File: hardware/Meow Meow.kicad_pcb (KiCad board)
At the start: 2 copper layers, 52.5 x 47.5 mm, 22 parts, among them P1 USB_micro, P2 UP, P3 LEFT, P4 CONN_02X03, P5 CLICK_LEFT, P6 RIGHT, P7 SPACE, SW1 RESET, U1 ATSAMD11C14A-SSUT, U2 AP2114-3.3K, Y1 32k

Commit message: Update componets
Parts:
- removed C3: 22pF, Capacitors_SMD:C_0805_HandSoldering
- removed Y1: 32k, Crystals:Crystal_Round_d3.0mm_Vertical
- added F1: 0.5A, Resistors_SMD:R_1812_HandSoldering, F.Cu at (164.0, 99.0)
- added P1: D, MeowMeow:ALLIGATORCLIP, F.Cu at (120.5, 67.7)
- added P10: A, MeowMeow:ALLIGATORCLIP, F.Cu at (145.8, 66.5)
- added P11: W, MeowMeow:ALLIGATORCLIP, F.Cu at (152.8, 67.0)
- added P12: MOUSE_LEFT, MeowMeow:ALLIGATORCLIP, F.Cu at (104.5, 68.0)
- added P13: CONN_01X12, Pin_Headers:Pin_Header_Straight_1x12_Pitch2.54mm, F.Cu at (120.0, 94.2)
- added P8: S, MeowMeow:ALLIGATORCLIP, F.Cu at (125.5, 68.0)
- C1: value 22pF -> C_Small
- D1: value LED -> POWER
- P2: value UP -> SPACE
- P3: value LEFT -> KEY_RIGHT_ARROW
- P5: value CLICK_LEFT -> KEY_LEFT_ARROW
- P6: value RIGHT -> KEY_DOWN_ARROW
- P7: value SPACE -> KEY_UP_ARROW
- P9: renamed from P1; value USB_micro -> USB_Micro
- SW1: value RESET -> SW_Push
- U1: value ATSAMD11C14A-SSUT -> ATSAMD21G15A-AU; footprint Housings_SOIC:SOIC-14_3.9x8.7mm_Pitch1.27mm -> Housings_QFP:TQFP-48_7x7mm_Pitch0.5mm
- moved P2 43.1 mm to (108.0, 67.7), turned to 0 degrees
- moved C2 34.4 mm to (149.0, 101.0)
- moved P7 33.6 mm to (137.8, 68.2)
- moved P6 30.3 mm to (131.5, 67.7)
- moved P5 30.3 mm to (116.2, 68.2)
- moved P3 22.0 mm to (111.0, 68.0)
- moved D2 10.2 mm to (128.0, 112.2)
- moved R3 10.2 mm to (129.3, 109.0)
- moved C1 6.53 mm to (141.5, 94.5), turned to 0 degrees
- moved R1 4.74 mm to (130.8, 120.4)
- moved SW1 4.74 mm to (127.5, 119.9)
- moved U1 2.21 mm to (141.5, 103.5)
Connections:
- C1 pad 1: GND -> Net-(C1-Pad1)
- C1 pad 2: /OSC1 -> GND
- C2 pad 1: Net-(C2-Pad1) -> +3V3
- D2 pad 2: /SWDIO -> /D8
- P2 pad 1: /X1/Y7 -> /Y4
- P3 pad 1: /X0/Y6 -> /Y3
- P5 pad 1: /Y3 -> /Y2
- P6 pad 1: /Y2 -> /Y1
- P9 pad 1: VCC -> Net-(F1-Pad2)
- P9 pad SHEL: GND -> (no net)
- R1 pad 1: Net-(C2-Pad1) -> Net-(R1-Pad1)
- R1 pad 2: /RESET -> Net-(R1-Pad2)
- SW1 pad 1: Net-(C2-Pad1) -> GND
- SW1 pad 2: GND -> Net-(R1-Pad1)
- U1 pad 1: /Y3 -> /SDA
- U1 pad 10: /D+ -> /Y3
- U1 pad 11: GND -> /Y4
- U1 pad 12: +3V3 -> /Y5
- U1 pad 13: /Y0 -> Net-(U1-Pad13)
- U1 pad 14: /Y2 -> Net-(U1-Pad14)
- U1 pad 2: /OSC1 -> /SCL
- U1 pad 3: /OSC2 -> /Y0
- U1 pad 4: /X0/Y6 -> /Y1
- U1 pad 5: /X1/Y7 -> GND
- U1 pad 6: /RESET -> +3V3
- U1 pad 7: /SWCLK -> /Y14
- U1 pad 8: /SWDIO -> /Y15
- U1 pad 9: /D- -> /Y2
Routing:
- net GND: track 196.1 -> 18.0 mm
- net +3V3: track 107.9 -> 58.6 mm
- net /Y0: track 34.2 -> 0.00 mm
- net /RESET: track 32.7 -> 0.00 mm
- net /X0/Y6: track 31.1 -> 0.00 mm
- net /Y2: track 29.1 -> 0.00 mm
- net /D+: track 25.5 -> 0.00 mm
- net /D-: track 23.1 -> 0.00 mm
- net /X1/Y7: track 21.5 -> 0.00 mm
- net (no net): track 0.00 -> 17.9 mm
- net /Y3: track 17.3 -> 0.00 mm
- net /SWCLK: track 12.3 -> 0.00 mm
- net /SWDIO: track 12.2 -> 0.06 mm
- net /OSC2: track 11.1 -> 0.00 mm
- net VCC: track 9.54 -> 0.18 mm
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- removed copper zone on F.Cu, net GND

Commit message: Update capacitor Vddcore and leds
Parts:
- C1: value C_Small -> 1uF
- D1, D2: footprint LEDs:LED-3MM -> LEDs:LED_0805_HandSoldering
- moved D1 6.44 mm to (152.5, 104.5)
- moved D2 6.27 mm to (129.2, 106.0)
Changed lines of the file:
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@@
-    )
-  )
-  (module LEDs:LED-3MM (layer F.Cu)
-    (at 153.59 110.85 180)
-    (descr "LED 3mm round vertical")
-    (tags "LED  3mm round vertical")
-    (fp_text reference D1 (at 1.91 3.06 180) (layer F.SilkS)
-      (effects (font (size 1 1) (thickness 0.15)))
-    )
-    (fp_text value POWER (at 1.3 -2.9 180) (layer F.Fab)
-      (effects (font (size 1 1) (thickness 0.15)))
-    )
-    (fp_line (start -1.2 2.3) (end 3.8 2.3) (layer F.CrtYd) (width 0.05))
-    (fp_line (start 3.8 2.3) (end 3.8 -2.2) (layer F.CrtYd) (width 0.05))
-    (fp_line (start 3.8 -2.2) (end -1.2 -2.2) (layer F.CrtYd) (width 0.05))
-    (fp_line (start -1.2 -2.2) (end -1.2 2.3) (layer F.CrtYd) (width 0.05))
-    (fp_line (start -0.199 1.314) (end -0.199 1.114) (layer F.SilkS) (width 0.15))
-    (fp_line (start -0.199 -1.28) (end -0.199 -1.1) (layer F.SilkS) (width 0.15))
-    (fp_arc (start 1.301 0.034) (end -0.199 -1.286) (angle 108.5) (layer F.SilkS) (width 0.15))
-    (fp_arc (start 1.301 0.034) (end 0.25 -1.1) (angle 85.7) (layer F.SilkS) (width 0.15))
-    (fp_arc (start 1.311 0.034) (end 3.051 0.994) (angle 110) (layer F.SilkS) (width 0.15))
-    (fp_arc (start 1.301 0.034) (end 2.335 1.094) (angle 87.5) (layer F.SilkS) (width 0.15))
-    (fp_text user K (at -1.69 1.74 180) (layer F.SilkS)
-      (effects (font (size 1 1) (thickness 0.15)))
-    )
-    (pad 1 thru_hole rect (at 0 0 270) (size 2 2) (drill 1.00076) (layers *.Cu *.Mask)
-      (net 4 "Net-(D1-Pad1)"))
-    (pad 2 thru_hole circle (at 2.54 0 180) (size 2 2) (drill 1.00076) (layers *.Cu *.Mask)
-      (net 3 +3V3))
-    (model LEDs.3dshapes/LED-3MM.wrl
-      (at (xyz 0.05 0 0))
-      (scale (xyz 1 1 1))
-      (rotate (xyz 0 0 90))
-    )
-  )
-  (module LEDs:LED-3MM (layer F.Cu)
-    (at 128.01 112.15)
-    (descr "LED 3mm round vertical")
-    (tags "LED  3mm round vertical")
-    (fp_text reference D2 (at 4.84 1.2) (layer F.SilkS)
-      (effects (font (size 1 1) (thickness 0.15)))
-    )
-    (fp_text value LED (at 1.3 -2.9) (layer F.Fab)
-      (effects (font (size 1 1) (thickness 0.15)))
-    )
-    (fp_line (start -1.2 2.3) (end 3.8 2.3) (layer F.CrtYd) (width 0.05))
-    (fp_line (start 3.8 2.3) (end 3.8 -2.2) (layer F.CrtYd) (width 0.05))
-    (fp_line (start 3.8 -2.2) (end -1.2 -2.2) (layer F.CrtYd) (width 0.05))
-    (fp_line (start -1.2 -2.2) (end -1.2 2.3) (layer F.CrtYd) (width 0.05))
-    (fp_line (start -0.199 1.314) (end -0.199 1.114) (layer F.SilkS) (width 0.15))
-    (fp_line (start -0.199 -1.28) (end -0.199 -1.1) (layer F.SilkS) (width 0.15))
-    (fp_arc (start 1.301 0.034) (end -0.199 -1.286) (angle 108.5) (layer F.SilkS) (width 0.15))
-    (fp_arc (start 1.301 0.034) (end 0.25 -1.1) (angle 85.7) (layer F.SilkS) (width 0.15))
-    (fp_arc (start 1.311 0.034) (end 3.051 0.994) (angle 110) (layer F.SilkS) (width 0.15))
-    (fp_arc (start 1.301 0.034) (end 2.335 1.094) (angle 87.5) (layer F.SilkS) (width 0.15))
-    (fp_text user K (at -0.66 -2.3) (layer F.SilkS)
-      (effects (font (size 1 1) (thickness 0.15)))
-    )
-    (pad 1 thru_hole rect (at 0 0 90) (size 2 2) (drill 1.00076) (layers *.Cu *.Mask)
-      (net 5 "Net-(D2-Pad1)"))
-    (pad 2 thru_hole circle (at 2.54 0) (size 2 2) (drill 1.00076) (layers *.Cu *.Mask)
-      (net 16 /D8))
-    (model LEDs.3dshapes/LED-3MM.wrl
-      (at (xyz 0.05 0 0))
-      (scale (xyz 1 1 1))
-      (rotate (xyz 0 0 90))
     )
   )
@@
       (effects (font (size 1 1) (thickness 0.15)))
     )
-    (fp_text value C_Small (at 0 1.75) (layer F.Fab)
+    (fp_text value 1uF (at 0 1.75) (layer F.Fab)
       (effects (font (size 1 1) (thickness 0.15)))
     )
@@
     )
   )
+  (module LEDs:LED_0805_HandSoldering (layer F.Cu)
+    (at 152.5 104.5 180)
+    (descr "Resistor SMD 0805, hand soldering")
+    (tags "resistor 0805")
+    (attr smd)
+    (fp_text reference D1 (at 0 -1.7 180) (layer F.SilkS)
+      (effects (font (size 1 1) (thickness 0.15)))
+    )
+    (fp_text value POWER (at 0 1.75 180) (layer F.Fab)
+      (effects (font (size 1 1) (thickness 0.15)))
+    )
+    (fp_line (start -0.4 -0.4) (end -0.4 0.4) (layer F.Fab) (width 0.1))
+    (fp_line (start -0.4 0) (end 0.2 -0.4) (layer F.Fab) (width 0.1))
+    (fp_line (start 0.2 0.4) (end -0.4 0) (layer F.Fab) (width 0.1))
+    (fp_line (start 0.2 -0.4) (end 0.2 0.4) (layer F.Fab) (width 0.1))
+    (fp_line (start -1 0.62) (end -1 -0.62) (layer F.Fab) (width 0.1))
+    (fp_line (start 1 0.62) (end -1 0.62) (layer F.Fab) (width 0.1))
+    (fp_line (start 1 -0.62) (end 1 0.62) (layer F.Fab) (width 0.1))
+    (fp_line (start -1 -0.62) (end 1 -0.62) (layer F.Fab) (width 0.1))
+    (fp_line (start 1 0.75) (end -2.2 0.75) (layer F.SilkS) (width 0.12))
+    (fp_line (start -2.2 -0.75) (end 1 -0.75) (layer F.SilkS) (width 0.12))
+    (fp_line (start -2.35 -0.9) (end 2.35 -0.9) (layer F.CrtYd) (width 0.05))
+    (fp_line (start -2.35 -0.9) (end -2.35 0.9) (layer F.CrtYd) (width 0.05))
+    (fp_line (start 2.35 0.9) (end 2.35 -0.9) (layer F.CrtYd) (width 0.05))
+    (fp_line (start 2.35 0.9) (end -2.35 0.9) (layer F.CrtYd) (width 0.05))
+    (fp_line (start -2.2 -0.75) (end -2.2 0.75) (layer F.SilkS) (width 0.12))
+    (pad 1 smd rect (at -1.35 0 180) (size 1.5 1.3) (layers F.Cu F.Paste F.Mask)
+      (net 4 "Net-(D1-Pad1)"))
+    (pad 2 smd rect (at 1.35 0 180) (size 1.5 1.3) (layers F.Cu F.Paste F.Mask)
+      (net 3 +3V3))
+    (model ${KISYS3DMOD}/LEDs.3dshapes/LED_0805.wrl
+      (at (xyz 0 0 0))
+      (scale (xyz 1 1 1))
+      (rotate (xyz 0 0 0))
+    )
+  )
+  (module LEDs:LED_0805_HandSoldering (layer F.Cu)
+    (at 129.25 106)
+    (descr "Resistor SMD 0805, hand soldering")
+    (tags "resistor 0805")
+    (attr smd)
+    (fp_text reference D2 (at 0 -1.7) (layer F.SilkS)
+      (effects (font (size 1 1) (thickness 0.15)))
+    )
+    (fp_text value LED (at 0 1.75) (layer F.Fab)
+      (effects (font (size 1 1) (thickness 0.15)))
+    )
+    (fp_line (start -0.4 -0.4) (end -0.4 0.4) (layer F.Fab) (width 0.1))
+    (fp_line (start -0.4 0) (end 0.2 -0.4) (layer F.Fab) (width 0.1))
+    (fp_line (start 0.2 0.4) (end -0.4 0) (layer F.Fab) (width 0.1))
+    (fp_line (start 0.2 -0.4) (end 0.2 0.4) (layer F.Fab) (width 0.1))
+    (fp_line (start -1 0.62) (end -1 -0.62) (layer F.Fab) (width 0.1))
+    (fp_line (start 1 0.62) (end -1 0.62) (layer F.Fab) (width 0.1))
+    (fp_line (start 1 -0.62) (end 1 0.62) (layer F.Fab) (width 0.1))
+    (fp_line (start -1 -0.62) (end 1 -0.62) (layer F.Fab) (width 0.1))
+    (fp_line (start 1 0.75) (end -2.2 0.75) (layer F.SilkS) (width 0.12))
+    (fp_line (start -2.2 -0.75) (end 1 -0.75) (layer F.SilkS) (width 0.12))
+    (fp_line (start -2.35 -0.9) (end 2.35 -0.9) (layer F.CrtYd) (width 0.05))
+    (fp_line (start -2.35 -0.9) (end -2.35 0.9) (layer F.CrtYd) (width 0.05))
+    (fp_line (start 2.35 0.9) (end 2.35 -0.9) (layer F.CrtYd) (width 0.05))
+    (fp_line (start 2.35 0.9) (end -2.35 0.9) (layer F.CrtYd) (width 0.05))
+    (fp_line (start -2.2 -0.75) (end -2.2 0.75) (layer F.SilkS) (width 0.12))
+    (pad 1 smd rect (at -1.35 0) (size 1.5 1.3) (layers F.Cu F.Paste F.Mask)
+      (net 5 "Net-(D2-Pad1)"))
+    (pad 2 smd rect (at 1.35 0) (size 1.5 1.3) (layers F.Cu F.Paste F.Mask)
+      (net 16 /D8))
+    (model ${KISYS3DMOD}/LEDs.3dshapes/LED_0805.wrl
+      (at (xyz 0 0 0))
+      (scale (xyz 1 1 1))
+      (rotate (xyz 0 0 0))
+    )
+  )
   (dimension 47.5 (width 0.3) (layer Margin)
     (gr_text "47.500 mm" (at 108.65 101.25 270) (layer Margin)
@@
   (segment (start 166.95 104.225) (end 163.3 104.225) (width 0.5) (layer F.Cu) (net 0))
   (segment (start 163.3 104.225) (end 163.15 104.375) (width 0.5) (layer F.Cu) (net 0))
+  (segment (start 128 112.14) (end 128.01 112.15) (width 0.5) (layer F.Cu) (net 0))
+  (segment (start 153.6 110.84) (end 153.59 110.85) (width 0.5) (layer F.Cu) (net 0))
   (segment (start 167.6 121.05) (end 167.6 112.625) (width 0.5) (layer B.Cu) (net 1))
   (segment (start 167.6 112.625) (end 166.95 111.975) (width 0.5) (layer B.Cu) (net 1))
@@
   (segment (start 169.05 116.5) (end 169.05 117) (width 0.5) (layer F.Cu) (net 3))
   (segment (start 162.403719 118.275071) (end 162.743719 118.615071) (width 0.5) (layer F.Cu) (net 3))
-  (segment (start 153.6 110.84) (end 153.59 110.85) (width 0.5) (layer F.Cu) (net 4))
-  (segment (start 128 112.14) (end 128.01 112.15) (width 0.5) (layer F.Cu) (net 5))
   (segment (start 140.55 114.57) (end 140.59 114.61) (width 0.5) (layer F.Cu) (net 6))
   (segment (start 127.297656 121.397656) (end 127.5 121.6) (width 0.5) (layer F.Cu) (net 49))

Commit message: Add figure
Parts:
- added G***: LOGO, TIH:electronic_cats_logo_8x6, B.Cu at (158.8, 126.9)
- added svg2mod: meowmeow, svg2mod, F.Cu at (142.5, 109.2)
- C1, C2, C4, C5, C6, D1, D2, F1, P1, P10, P11, P12, P2, P3, P4, P5, P6, P7, P8, P9, R1, R2, R3, SW1, U1, U2: moved to B.Cu
- moved P8 83.9 mm to (179.6, 132.0), turned to 90 degrees
- moved P1 81.9 mm to (182.3, 121.4), turned to 90 degrees
- moved P13 80.7 mm to (198.8, 76.5)
- moved P5 76.0 mm to (179.1, 110.9), turned to 90 degrees
- moved P10 69.3 mm to (180.1, 126.6), turned to 90 degrees
- moved P7 68.0 mm to (103.8, 127.2), turned to 90 degrees
- moved P3 65.6 mm to (102.9, 133.1), turned to 90 degrees
- moved P4 59.1 mm to (183.3, 73.7)
- moved P11 56.8 mm to (179.7, 117.0), turned to 90 degrees
- moved P6 55.8 mm to (103.2, 115.9), turned to 270 degrees
- moved P2 53.8 mm to (102.6, 121.2), turned to 90 degrees
- moved P12 42.3 mm to (104.1, 110.3), turned to 90 degrees
- moved C6 41.0 mm to (124.9, 116.0)
- moved C5 35.1 mm to (127.8, 116.1)
- moved F1 33.3 mm to (130.7, 99.9), turned to 180 degrees
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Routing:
- net +3V3: track 58.6 -> 0.00 mm, vias 2 -> 0
- net GND: track 18.0 -> 0.00 mm, vias 1 -> 0
- net (no net): track 17.9 -> 0.00 mm
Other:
- board size 52.5 x 47.5 mm -> 98.7 x 61 mm
- board text added: "Meow Meow"
- board text added: "https://github.com/ElectronicCats/MeowMeow"
- board text added: "v 1.0"

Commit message: Update PCB
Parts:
- added G***: LOGO, LOGO, B.Cu at (127.7, 125.2)
- P1, P10, P11, P12, P2, P3, P5, P6, P7, P8: footprint MeowMeow:ALLIGATORCLIP -> Connectors:SEWALLI; moved to F.Cu
- P13: value CONN_01X12 -> Expansion; footprint Pin_Headers:Pin_Header_Straight_1x12_Pitch2.54mm -> Pines:610X1221121; moved to B.Cu
- P4: value CONN_02X03 -> SWD; footprint Pin_Headers:Pin_Header_Straight_2x03_Pitch2.54mm -> Pines:61000418321
- moved P1 81.3 mm to (101.9, 133.1), turned to 0 degrees
- moved P6 79.7 mm to (182.8, 111.2), turned to 0 degrees
- moved P3 79.1 mm to (182.1, 132.6), turned to 0 degrees
- moved P10 68.9 mm to (114.3, 106.4), turned to 0 degrees
- moved P4 63.8 mm to (142.4, 122.8), turned to 0 degrees
- moved P12 63.4 mm to (164.2, 130.7), turned to 180 degrees
- moved P8 60.0 mm to (119.7, 129.3), turned to 180 degrees
- moved P13 50.7 mm to (165.5, 114.8), turned to 270 degrees
- moved P7 16.1 mm to (102.8, 111.1), turned to 0 degrees
- moved P5 12.8 mm to (185.4, 122.0), turned to 0 degrees
- moved P11 12.3 mm to (172.8, 106.7), turned to 0 degrees
- moved D2 4.09 mm to (152.8, 110.5)
- moved R3 3.51 mm to (153.3, 114.5)
- moved P2 3.02 mm to (99.6, 121.9), turned to 0 degrees
- moved G*** 2.54 mm to (157.9, 124.6)
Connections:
- P13 pad 1: +3V3 -> /MOSI
- P13 pad 10: /TX/X2 -> /CS
- P13 pad 11: /I2S_D1/X7 -> +3V3
- P13 pad 12: /I2S_SCK -> GND
- P13 pad 2: GND -> /I2S_SCK
- P13 pad 3: /SCL -> /MISO
- P13 pad 4: /SDA -> /I2S_D1/X7
- P13 pad 5: /CS -> /SCK
- P13 pad 6: /SCK -> /TX/X2
- P13 pad 7: /MISO -> /SDA
- P13 pad 8: /MOSI -> /RX/X3
- P13 pad 9: /RX/X3 -> /SCL
- P4 pad 2: GND -> /SWCLK
- P4 pad 3: Net-(P4-Pad3) -> +3V3
- P4 pad 4: +3V3 -> GND

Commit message: PCB update
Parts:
- P1, P10, P11, P12, P2, P3, P5, P6, P7, P8: footprint Connectors:SEWALLI -> Connectors_EC:SEWALLI_renew
- moved P7 80.4 mm to (183.2, 110.5), turned to 90 degrees
- moved P3 79.9 mm to (102.2, 131.7), turned to 270 degrees
- moved P5 66.4 mm to (119.7, 131.2)
- moved P12 64.5 mm to (103.0, 110.3), turned to 90 degrees
- moved P8 63.6 mm to (183.3, 131.8), turned to 90 degrees
- moved P1 62.9 mm to (164.8, 132.0)
- moved P11 58.6 mm to (114.3, 105.4), turned to 270 degrees
- moved P10 56.4 mm to (170.6, 106.0), turned to 90 degrees
- moved P13 25.3 mm to (142.3, 124.9), turned to 0 degrees
- moved P4 20.5 mm to (161.0, 114.1), turned to 270 degrees
- moved P6 10.4 mm to (185.7, 121.2), turned to 90 degrees
- moved C4 2.72 mm to (127.6, 103.2)
- moved U2 1.46 mm to (126.2, 109.7)
- moved U1 1.23 mm to (143.4, 112.0)
- moved P2 1.01 mm to (99.3, 120.9), turned to 270 degrees

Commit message: added new connector
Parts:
- moved P3 85.3 mm to (184.8, 110.4), turned to 90 degrees
- moved P7 67.6 mm to (115.6, 106.9), turned to 270 degrees
- moved P5 65.1 mm to (184.8, 132.1), turned to 90 degrees
- moved P10 54.7 mm to (121.9, 130.8)
- moved P11 29.7 mm to (100.7, 131.9), turned to 90 degrees
- moved P1 25.3 mm to (187.6, 121.1), turned to 90 degrees
- moved P6 21.5 mm to (169.6, 107.0), turned to 270 degrees
- moved P8 19.2 mm to (164.2, 129.7), turned to 270 degrees
- moved P12 2.53 mm to (100.5, 110.1), turned to 270 degrees
- moved P2 1.40 mm to (97.9, 121.0), turned to 90 degrees

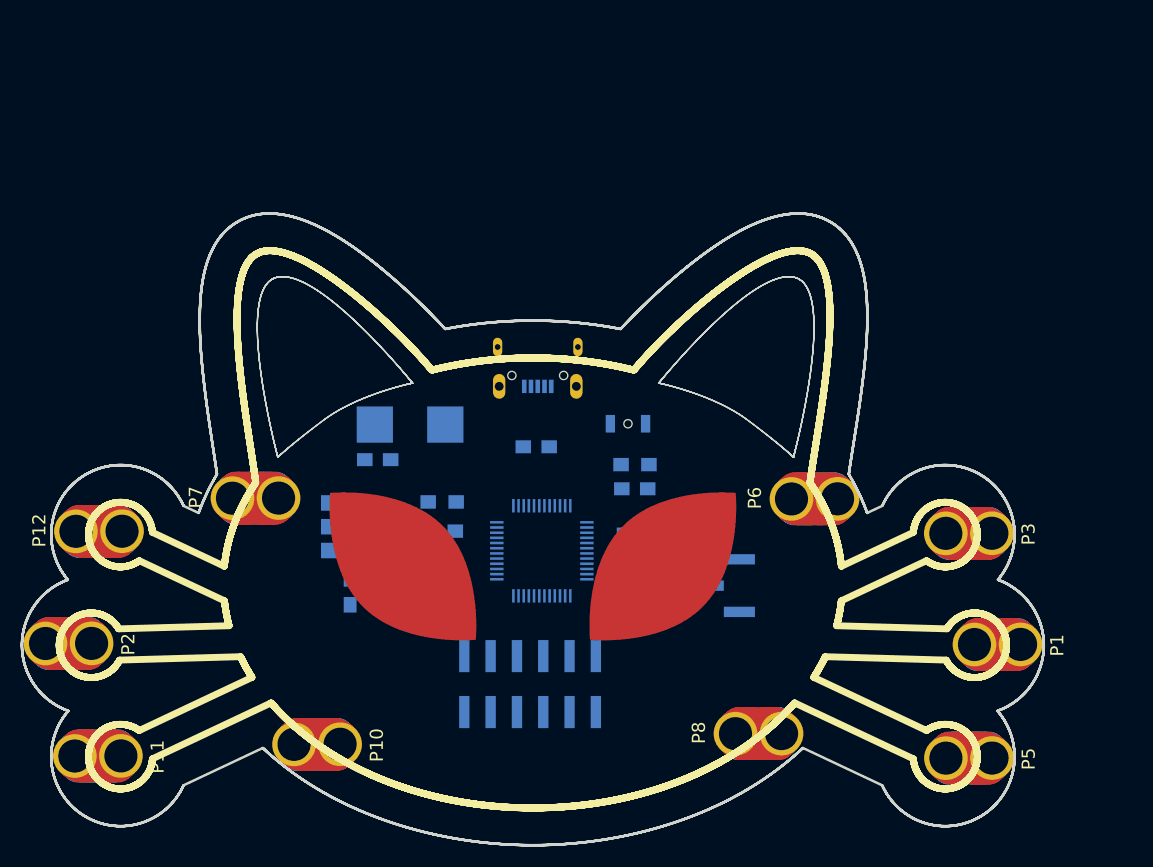
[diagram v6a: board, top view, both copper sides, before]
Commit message: Add logos
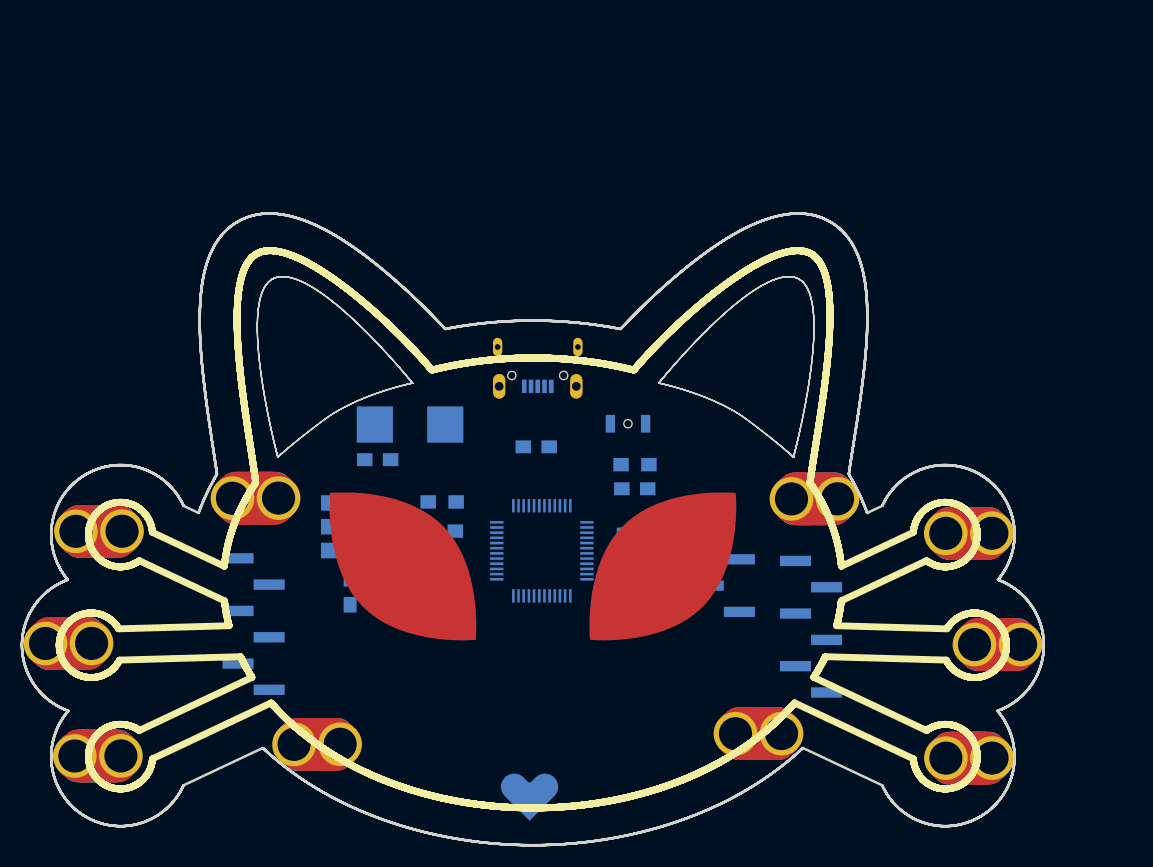
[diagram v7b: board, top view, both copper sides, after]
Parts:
- added G***: LOGO, LOGO, B.Cu at (143.3, 129.3)
- added P14: CONN_01X06, Pines:61000618321, B.Cu at (169.4, 119.4)
- added REF***: WEEE-Logo_4.2x6mm_SilkScreen, Symbols:WEEE-Logo_4.2x6mm_SilkScreen, B.Cu at (114.2, 97.9)
- added svg2mod: G***, svg2mod, B.Cu at (137.2, 93.7)
- added svg2mod: G***, svg2mod, B.Cu at (156.8, 99.8)
- added svg2mod: G***, svg2mod, B.Cu at (136.7, 107.5)
- added svg2mod: G***, svg2mod, B.Cu at (156.0, 110.2)
- added svg2mod: G***, svg2mod, B.Cu at (142.2, 135.9)
- P13: value Expansion -> CONN_01X06; footprint Pines:610X1221121 -> Pines:61000618321
- U1: value ATSAMD21G15A-AU -> ATSAMD21G18A-AU
- moved G*** 51.7 mm to (106.7, 117.3)
- moved P13 27.3 mm to (115.6, 119.1), turned to 90 degrees
- moved G*** 20.8 mm to (106.9, 125.0)
- moved R3 1.63 mm to (152.8, 113.0)
- renumbered SW1 to RESET
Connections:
- P13 pad 2: /I2S_SCK -> /MISO
- P13 pad 3: /MISO -> /SCK
- P13 pad 4: /I2S_D1/X7 -> /SDA
- P13 pad 5: /SCK -> /SCL
- P13 pad 6: /TX/X2 -> +3V3
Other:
- board text added: "Made with in México"
- board text added: "electroniccats.com/howtomeow"
- board text removed: "https://github.com/ElectronicCats/MeowMeow"
